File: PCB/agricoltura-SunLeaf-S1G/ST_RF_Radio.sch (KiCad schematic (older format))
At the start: 1 part

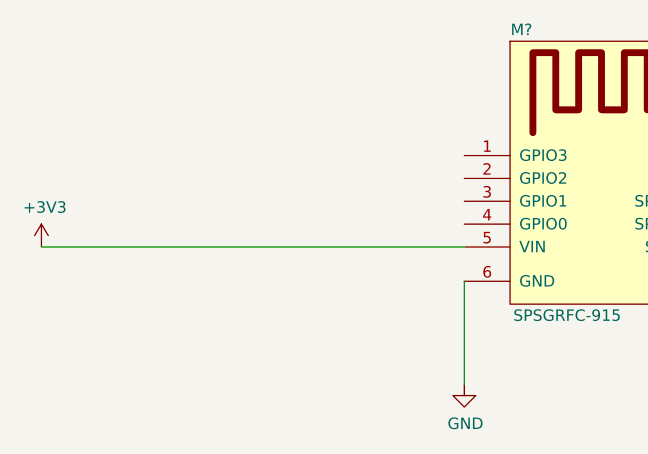
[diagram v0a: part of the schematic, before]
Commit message: Power Supply and Datasheets
Added datasheets for parts in use, designed power supply circuit
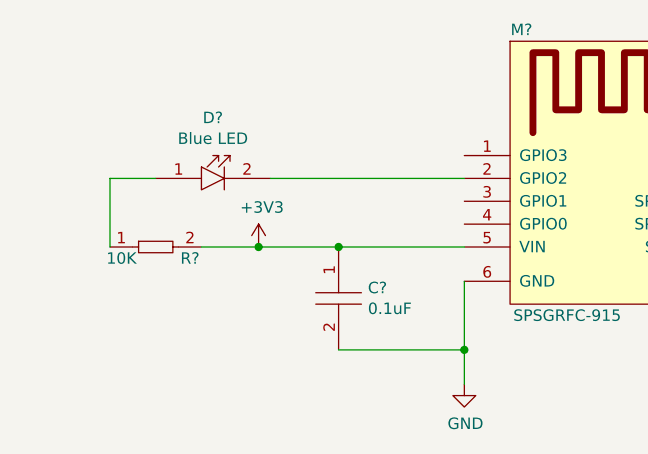
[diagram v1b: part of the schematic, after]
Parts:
- added C?: C0402C104K9PACTU, AVR-KiCAD-Lib-Resistors:R0402, symbol AVR-KiCAD-Lib-Capacitors:C0402C104K9PACTU
- added D?: LTST-C194TBKT, AVR-KiCAD-Lib-Diodes:LED0603, symbol AVR-KiCAD-Lib-Diodes:LTST-C194TBKT
- added R?: RC0402FR-0710KL, AVR-KiCAD-Lib-Resistors:R0402, symbol AVR-KiCAD-Lib-Resistors:RC0402FR-0710KL
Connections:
- net +3V3: now also C?.1, R?.2
- net GND: now also C?.2
- net at M?.2 (GPIO2): now also D?.2
- new net: D?.1, R?.1
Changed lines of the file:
@@
 	6650 3500 10350 3500
 Wire Wire Line
-	5350 3500 3500 3500
+	5350 3500 4800 3500
 $Comp
 L power:+3V3 #PWR?
 U 1 1 5F0903F3
-P 3500 3500
-F 0 "#PWR?" H 3500 3350 50  0001 C CNN
-F 1 "+3V3" H 3515 3673 50  0000 C CNN
-F 2 "" H 3500 3500 50  0001 C CNN
-F 3 "" H 3500 3500 50  0001 C CNN
-	1    3500 3500
+P 4450 3500
+F 0 "#PWR?" H 4450 3350 50  0001 C CNN
+F 1 "+3V3" H 4465 3673 50  0000 C CNN
+F 2 "" H 4450 3500 50  0001 C CNN
+F 3 "" H 4450 3500 50  0001 C CNN
+	1    4450 3500
 	1    0    0    -1
 $EndComp
@@
 $EndComp
 Wire Wire Line
-	5350 3650 5350 4100
+	5350 3650 5350 3950
+$Comp
+L AVR-KiCAD-Lib-Diodes:LTST-C194TBKT D?
+U 1 1 5F146E50
+P 4250 3200
+F 0 "D?" H 4250 3465 50  0000 C CNN
+F 1 "LTST-C194TBKT" H 4300 3400 50  0001 C CNN
+F 2 "AVR-KiCAD-Lib-Diodes:LED0603" H 4200 3050 50  0001 C CNN
+F 3 "http://optoelectronics.liteon.com/upload/download/DS22-2010-0025/LTST-C194TBKT.PDF" H 4150 3300 50  0001 C CNN
+F 4 "0.42000" H 4350 3450 50  0001 C CNN "Cost QTY: 1"
+F 5 "0.07797" H 4450 3550 50  0001 C CNN "Cost QTY: 1000"
+F 6 "*" H 4550 3650 50  0001 C CNN "Cost QTY: 2500"
+F 7 "0.06102" H 4650 3750 50  0001 C CNN "Cost QTY: 5000"
+F 8 "0.05424" H 4750 3850 50  0001 C CNN "Cost QTY: 10000"
+F 9 "Lite-On Inc." H 4850 3950 50  0001 C CNN "MFR"
+F 10 "LTST-C194TBKT" H 4950 4050 50  0001 C CNN "MFR#"
+F 11 "Digikey" H 5050 4150 50  0001 C CNN "Vendor"
+F 12 "160-1837-2-ND" H 5150 4250 50  0001 C CNN "Vendor #"
+F 13 "AVR" H 5250 4350 50  0001 C CNN "Designer"
+F 14 "0.45mm" H 5350 4450 50  0001 C CNN "Height"
+F 15 "3/1/2020" H 6450 5550 50  0001 C CNN "Date Created"
+F 16 "3/1/2020" H 5450 4550 50  0001 C CNN "Date Modified"
+F 17 "Yes" H 5550 4650 50  0001 C CNN "Lead-Free ?"
+F 18 "1" H 5650 4750 50  0001 C CNN "RoHS Levels"
+F 19 "SMT" H 5750 4850 50  0001 C CNN "Mounting"
+F 20 "2" H 5850 4950 50  0001 C CNN "Pin Count #"
+F 21 "Active" H 5950 5050 50  0001 C CNN "Status"
+F 22 "*" H 6050 5150 50  0001 C CNN "Tolerance"
+F 23 "Blue LED Colorless" H 6150 5250 50  0001 C CNN "Type"
+F 24 "3.3V" H 6250 5350 50  0001 C CNN "Voltage"
+F 25 "0603" H 6350 5500 50  0001 C CNN "Package"
+F 26 "Blue 468nm LED Indication - Discrete 3.3V 0603 (1608 Metric)" H 6650 5800 50  0001 C CNN "Description"
+F 27 "Blue LED" H 4250 3374 50  0000 C CNN "_Value_"
+F 28 "*" H 6650 5800 50  0001 C CNN "Management_ID"
+	1    4250 3200
+	1    0    0    -1
+$EndComp
+$Comp
+L AVR-KiCAD-Lib-Resistors:RC0402FR-0710KL R?
+U 1 1 5F14CD98
+P 4000 3500
+F 0 "R?" H 4150 3450 50  0000 C CNN
+F 1 "RC0402FR-0710KL" H 4000 3725 50  0001 C CNN
+F 2 "AVR-KiCAD-Lib-Resistors:R0402" H 4000 3500 50  0001 C CNN
+F 3 "https://www.yageo.com/upload/media/product/productsearch/datasheet/rchip/PYu-RC_Group_51_RoHS_L_10.pdf" H 4000 3500 50  0001 C CNN
+F 4 "0.10000" H 4100 3750 50  0001 C CNN "Cost QTY: 1"
+F 5 "0.00289" H 4200 3850 50  0001 C CNN "Cost QTY: 1000"
+F 6 "0.00251" H 4300 3950 50  0001 C CNN "Cost QTY: 2500"
+F 7 "0.00207" H 4400 4050 50  0001 C CNN "Cost QTY: 5000"
+F 8 "*" H 4500 4150 50  0001 C CNN "Cost QTY: 10000"
+F 9 "Yageo" H 4600 4250 50  0001 C CNN "MFR"
+F 10 "RC0402FR-0710KL" H 4700 4350 50  0001 C CNN "MFR#"
+F 11 "Digikey" H 4800 4450 50  0001 C CNN "Vendor"
+F 12 "311-10.0KLRCT-ND" H 4900 4550 50  0001 C CNN "Vendor #"
+F 13 "AVR" H 5000 4650 50  0001 C CNN "Designer"
+F 14 "0.4mm" H 5100 4750 50  0001 C CNN "Height"
+F 15 "12/11/2019" H 6200 5850 50  0001 C CNN "Date Created"
+F 16 "12/11/2019" H 5200 4850 50  0001 C CNN "Date Modified"
+F 17 "Yes" H 5300 4950 50  0001 C CNN "Lead-Free ?"
+F 18 "1" H 5400 5050 50  0001 C CNN "RoHS Levels"
+F 19 "SMT" H 5500 5150 50  0001 C CNN "Mounting"
+F 20 "2" H 5600 5250 50  0001 C CNN "Pin Count #"
+F 21 "Active" H 5700 5350 50  0001 C CNN "Status"
+F 22 "1%" H 5800 5450 50  0001 C CNN "Tolerance"
+F 23 "Thick FIlm Resistor" H 5900 5550 50  0001 C CNN "Type"
+F 24 "*" H 6000 5650 50  0001 C CNN "Voltage"
+F 25 "0402" H 6100 5800 50  0001 C CNN "Package"
+F 26 "10K" H 3850 3450 50  0000 C CNN "_Value_"
+F 27 "*" H 6400 6100 50  0001 C CNN "Management_ID"
+F 28 "10 kOhms ±1% 0.063W, 1/16W Chip Resistor 0402 (1005 Metric) Moisture Resistant Thick Film" H 6400 6100 50  0001 C CNN "Description"
+	1    4000 3500
+	1    0    0    -1
+$EndComp
+Wire Wire Line
+	4200 3500 4450 3500
+Connection ~ 4450 3500
+Wire Wire Line
+	3800 3500 3800 3200
+Wire Wire Line
+	3800 3200 4000 3200
+Wire Wire Line
+	4500 3200 5350 3200
+$Comp
+L AVR-KiCAD-Lib-Capacitors:C0402C104K9PACTU C?
+U 1 1 5F154BB5
+P 4800 3700
+F 0 "C?" V 4779 3828 50  0000 L CNN
+F 1 "C0402C104K9PACTU" H 4850 3900 50  0001 C CNN
+F 2 "AVR-KiCAD-Lib-Resistors:R0402" H 4600 3700 50  0001 C CNN
+F 3 "https://content.kemet.com/datasheets/KEM_C1006_X5R_SMD.pdf" H 4700 3800 50  0001 C CNN
+F 4 "0.10000" H 4900 3950 50  0001 C CNN "Cost QTY: 1"
+F 5 "0.01139" H 5000 4050 50  0001 C CNN "Cost QTY: 1000"
+F 6 "0.01035" H 5100 4150 50  0001 C CNN "Cost QTY: 2500"
+F 7 "0.00952" H 5200 4250 50  0001 C CNN "Cost QTY: 5000"
+F 8 "0.00756" H 5300 4350 50  0001 C CNN "Cost QTY: 10000"
+F 9 "KEMET" H 5400 4450 50  0001 C CNN "MFR"
+F 10 "C0402C104K9PACTU" H 5500 4550 50  0001 C CNN "MFR#"
+F 11 "Digikey" H 5600 4650 50  0001 C CNN "Vendor"
+F 12 "399-3026-6-ND" H 5700 4750 50  0001 C CNN "Vendor #"
+F 13 "AVR" H 5800 4850 50  0001 C CNN "Designer"
+F 14 "0.55mm" H 5900 4950 50  0001 C CNN "Height"
+F 15 "12/7/2019" H 7000 6050 50  0001 C CNN "Date Created"
+F 16 "12/7/2019" H 6000 5050 50  0001 C CNN "Date Modified"
+F 17 "Yes" H 6100 5150 50  0001 C CNN "Lead-Free ?"
+F 18 "1" H 6200 5250 50  0001 C CNN "RoHS Levels"
+F 19 "SMT" H 6300 5350 50  0001 C CNN "Mounting"
+F 20 "2" H 6400 5450 50  0001 C CNN "Pin Count #"
+F 21 "Active" H 6500 5550 50  0001 C CNN "Status"
+F 22 "10%" H 6600 5650 50  0001 C CNN "Tolerance"
+F 23 "Ceramic Cap" H 6700 5750 50  0001 C CNN "Type"
+F 24 "6.3V" H 6800 5850 50  0001 C CNN "Voltage"
+F 25 "0402" H 6900 6000 50  0001 C CNN "Package"
+F 26 "0.1µF ±10% 6.3V Ceramic Capacitor X5R 0402 (1005 Metric)" H 7300 6400 50  0001 C CNN "Description"
+F 27 "0.1uF" V 4870 3828 50  0000 L CNN "_Value_"
+F 28 "*" H 7200 6300 50  0001 C CNN "Management_ID"
+	1    4800 3700
+	0    1    1    0
+$EndComp
+Connection ~ 4800 3500
+Wire Wire Line
+	4800 3500 4450 3500
+Wire Wire Line
+	4800 3950 5350 3950
+Connection ~ 5350 3950
+Wire Wire Line
+	5350 3950 5350 4100
 $EndSCHEMATC

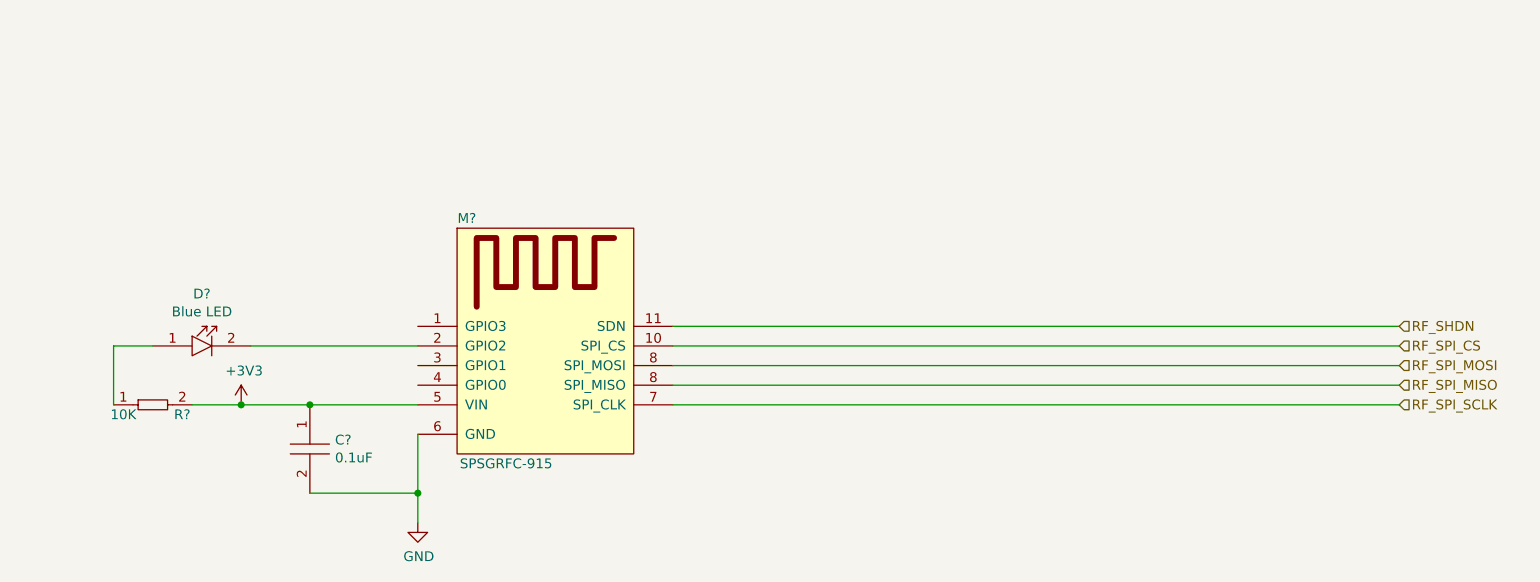
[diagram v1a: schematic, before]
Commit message: Schematic Complete
Schematic completed and PCB started
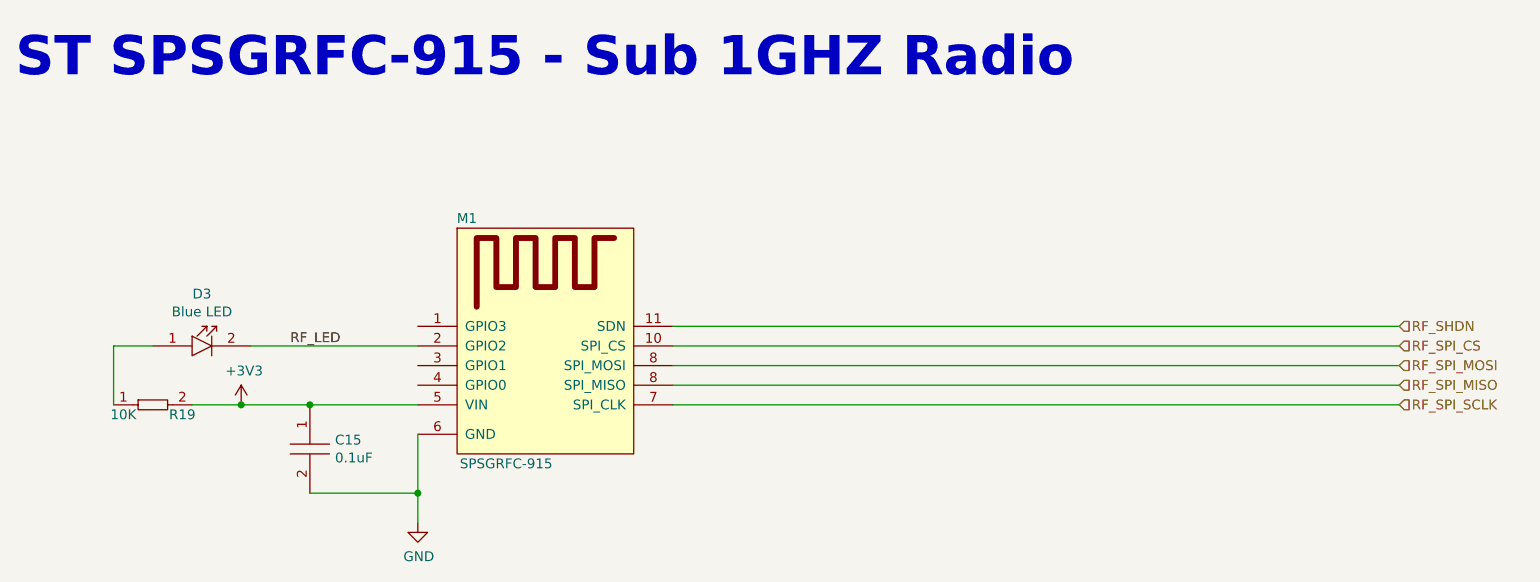
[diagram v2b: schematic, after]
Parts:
- gave numbers to parts that had none: 4
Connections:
- net RF_LED: now reaches D3.2, M1.2 (GPIO2)
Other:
- note added: "ST SPSGRFC-915 - Sub 1GHZ Radio"
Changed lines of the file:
@@
 $EndDescr
 $Comp
-L AVR-KiCAD-Lib-Modules:SPSGRFC-915 M?
+L AVR-KiCAD-Lib-Modules:SPSGRFC-915 M1
 U 1 1 5F088F18
 P 5550 2600
-F 0 "M?" H 5600 2650 50  0000 C CNN
+F 0 "M1" H 5600 2650 50  0000 C CNN
 F 1 "SPSGRFC-915" H 5600 2800 50  0001 C CNN
 F 2 "AVR-KiCAD-Lib-Modules:XCVR_SPSGRF-915" H 7600 5350 50  0001 C CNN
@@
 	5350 3500 4800 3500
 $Comp
-L power:+3V3 #PWR?
+L power:+3V3 #PWR020
 U 1 1 5F0903F3
 P 4450 3500
-F 0 "#PWR?" H 4450 3350 50  0001 C CNN
+F 0 "#PWR020" H 4450 3350 50  0001 C CNN
 F 1 "+3V3" H 4465 3673 50  0000 C CNN
 F 2 "" H 4450 3500 50  0001 C CNN
@@
 $EndComp
 $Comp
-L power:GND #PWR?
+L power:GND #PWR021
 U 1 1 5F090A88
 P 5350 4100
-F 0 "#PWR?" H 5350 3850 50  0001 C CNN
+F 0 "#PWR021" H 5350 3850 50  0001 C CNN
 F 1 "GND" H 5355 3927 50  0000 C CNN
 F 2 "" H 5350 4100 50  0001 C CNN
@@
 	5350 3650 5350 3950
 $Comp
-L AVR-KiCAD-Lib-Diodes:LTST-C194TBKT D?
+L AVR-KiCAD-Lib-Diodes:LTST-C194TBKT D3
 U 1 1 5F146E50
 P 4250 3200
-F 0 "D?" H 4250 3465 50  0000 C CNN
+F 0 "D3" H 4250 3465 50  0000 C CNN
 F 1 "LTST-C194TBKT" H 4300 3400 50  0001 C CNN
 F 2 "AVR-KiCAD-Lib-Diodes:LED0603" H 4200 3050 50  0001 C CNN
@@
 $EndComp
 $Comp
-L AVR-KiCAD-Lib-Resistors:RC0402FR-0710KL R?
+L AVR-KiCAD-Lib-Resistors:RC0402FR-0710KL R19
 U 1 1 5F14CD98
 P 4000 3500
-F 0 "R?" H 4150 3450 50  0000 C CNN
+F 0 "R19" H 4150 3450 50  0000 C CNN
 F 1 "RC0402FR-0710KL" H 4000 3725 50  0001 C CNN
 F 2 "AVR-KiCAD-Lib-Resistors:R0402" H 4000 3500 50  0001 C CNN
@@
 	4500 3200 5350 3200
 $Comp
-L AVR-KiCAD-Lib-Capacitors:C0402C104K9PACTU C?
+L AVR-KiCAD-Lib-Capacitors:C0402C104K9PACTU C15
 U 1 1 5F154BB5
 P 4800 3700
-F 0 "C?" V 4779 3828 50  0000 L CNN
+F 0 "C15" V 4779 3828 50  0000 L CNN
 F 1 "C0402C104K9PACTU" H 4850 3900 50  0001 C CNN
 F 2 "AVR-KiCAD-Lib-Resistors:R0402" H 4600 3700 50  0001 C CNN
@@
 Wire Wire Line
 	5350 3950 5350 4100
+Text Label 4700 3200 0    50   ~ 0
+RF_LED
+Text Notes 3300 1850 0    200  ~ 40
+ST SPSGRFC-915 - Sub 1GHZ Radio
 $EndSCHEMATC

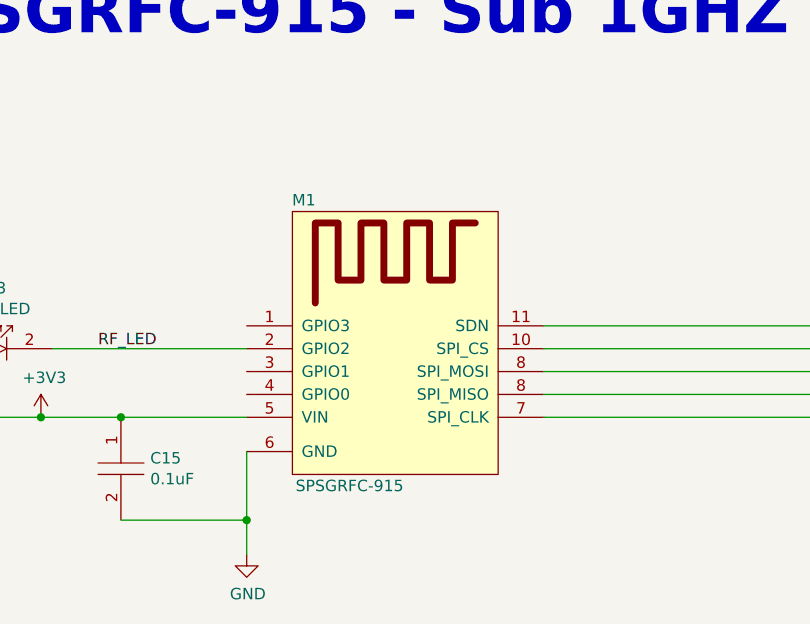
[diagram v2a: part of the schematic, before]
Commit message: PCB Progress
added TVS diodes fo QWIIC connector serial signals. Did more routing overall.
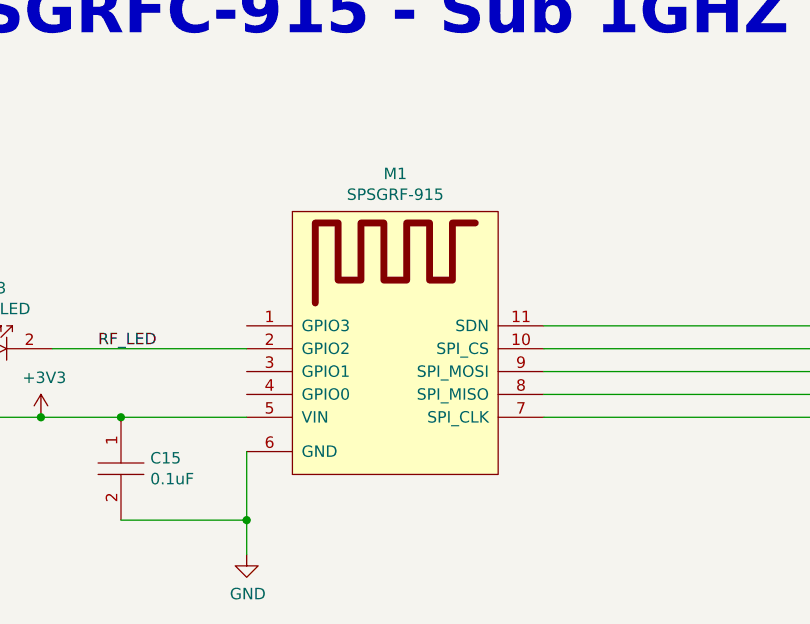
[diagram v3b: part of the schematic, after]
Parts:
- removed M1: SPSGRFC-915, AVR-KiCAD-Lib-Modules:XCVR_SPSGRF-915, symbol AVR-KiCAD-Lib-Modules:SPSGRFC-915
- added M1: SPSGRF-915, AVR-KiCAD-Lib-Modules:XCVR_SPSGRF-915, symbol AVR-KiCAD-Lib-Modules:SPSGRF-915
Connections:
- net +3V3: now also M1.5 (VIN)
- net GND: now also M1.6 (GND)
- net RF_LED: now also M1.2 (GPIO2)
- net RF_SHDN: now also M1.11 (SDN)
- net RF_SPI_CS: now also M1.10 (SPI_CS)
- net RF_SPI_MISO: now also M1.8 (SPI_MISO)
- net RF_SPI_MOSI: now also M1.9 (SPI_MOSI)
- net RF_SPI_SCLK: now also M1.7 (SPI_CLK)
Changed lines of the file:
@@
 Comment4 ""
 $EndDescr
-$Comp
-L AVR-KiCAD-Lib-Modules:SPSGRFC-915 M1
-U 1 1 5F088F18
-P 5550 2600
-F 0 "M1" H 5600 2650 50  0000 C CNN
-F 1 "SPSGRFC-915" H 5600 2800 50  0001 C CNN
-F 2 "AVR-KiCAD-Lib-Modules:XCVR_SPSGRF-915" H 7600 5350 50  0001 C CNN
-F 3 "https://www.st.com/content/ccc/resource/technical/document/datasheet/group3/21/ae/a6/78/64/3b/46/5d/DM00347814/files/DM00347814.pdf/jcr:content/translations/en.DM00347814.pdf" H 5450 2700 50  0001 C CNN
-F 4 "12.35000" H 5650 2850 50  0001 C CNN "Cost QTY: 1"
-F 5 "7.82040" H 5750 2950 50  0001 C CNN "Cost QTY: 1000"
-F 6 "*" H 5850 3050 50  0001 C CNN "Cost QTY: 2500"
-F 7 "7.29120" H 5950 3150 50  0001 C CNN "Cost QTY: 5000"
-F 8 "7.05600" H 6050 3250 50  0001 C CNN "Cost QTY: 10000"
-F 9 "STMicroelectronics" H 6150 3350 50  0001 C CNN "MFR"
-F 10 "SPSGRFC-915" H 6250 3450 50  0001 C CNN "MFR#"
-F 11 "Digikey" H 6350 3550 50  0001 C CNN "Vendor"
-F 12 "497-17226-ND" H 6450 3650 50  0001 C CNN "Vendor #"
-F 13 "AVR" H 6550 3750 50  0001 C CNN "Designer"
-F 14 "2mm" H 6650 3850 50  0001 C CNN "Height"
-F 15 "6/4/2020" H 7750 4950 50  0001 C CNN "Date Created"
-F 16 "6/4/2020" H 6750 3950 50  0001 C CNN "Date Modified"
-F 17 "Yes" H 6850 4050 50  0001 C CNN "Lead-Free ?"
-F 18 "1" H 6950 4150 50  0001 C CNN "RoHS Levels"
-F 19 "SMT" H 7050 4250 50  0001 C CNN "Mounting"
-F 20 "11" H 7150 4350 50  0001 C CNN "Pin Count #"
-F 21 "Active" H 7250 4450 50  0001 C CNN "Status"
-F 22 "*" H 7350 4550 50  0001 C CNN "Tolerance"
-F 23 "SoM" H 7450 4650 50  0001 C CNN "Type"
-F 24 "1.8V ~ 3.6V" H 7550 4750 50  0001 C CNN "Voltage"
-F 25 "Proprietary Module" H 7650 4900 50  0001 C CNN "Package"
-F 26 "General ISM < 1GHz  Transceiver Module 433MHz, 868MHz, 915MHz Antenna Not Included, U.FL Surface Mount" H 7950 5200 50  0001 C CNN "Description"
-F 27 "SPSGRFC-915" H 5800 1400 50  0000 C CNN "_Value_"
-F 28 "*" H 7950 5200 50  0001 C CNN "Management_ID"
-	1    5550 2600
-	1    0    0    -1
-$EndComp
 Text HLabel 10350 3100 2    50   Input ~ 0
 RF_SHDN
@@
 Text Notes 3300 1850 0    200  ~ 40
 ST SPSGRFC-915 - Sub 1GHZ Radio
+$Comp
+L AVR-KiCAD-Lib-Modules:SPSGRF-915 M1
+U 1 1 5F42ADCA
+P 5550 2600
+F 0 "M1" H 6000 2765 50  0000 C CNN
+F 1 "SPSGRF-915" H 5600 2800 50  0001 C CNN
+F 2 "AVR-KiCAD-Lib-Modules:XCVR_SPSGRF-915" H 7600 5350 50  0001 C CNN
+F 3 "https://www.st.com/content/ccc/resource/technical/document/datasheet/f9/a3/aa/67/de/86/4b/62/DM00171035.pdf/files/DM00171035.pdf/jcr:content/translations/en.DM00171035.pdf" H 5450 2700 50  0001 C CNN
+F 4 "15.79000" H 5650 2850 50  0001 C CNN "Cost QTY: 1"
+F 5 "10.00160" H 5750 2950 50  0001 C CNN "Cost QTY: 1000"
+F 6 "*" H 5850 3050 50  0001 C CNN "Cost QTY: 2500"
+F 7 "9.32480" H 5950 3150 50  0001 C CNN "Cost QTY: 5000"
+F 8 "9.02400" H 6050 3250 50  0001 C CNN "Cost QTY: 10000"
+F 9 "STMicroelectronics" H 6150 3350 50  0001 C CNN "MFR"
+F 10 "SPSGRF-915" H 6250 3450 50  0001 C CNN "MFR#"
+F 11 "Digikey" H 6350 3550 50  0001 C CNN "Vendor"
+F 12 "497-15956-ND" H 6450 3650 50  0001 C CNN "Vendor #"
+F 13 "AVR" H 6550 3750 50  0001 C CNN "Designer"
+F 14 "2mm" H 6650 3850 50  0001 C CNN "Height"
+F 15 "6/4/2020" H 7750 4950 50  0001 C CNN "Date Created"
+F 16 "6/4/2020" H 6750 3950 50  0001 C CNN "Date Modified"
+F 17 "Yes" H 6850 4050 50  0001 C CNN "Lead-Free ?"
+F 18 "1" H 6950 4150 50  0001 C CNN "RoHS Levels"
+F 19 "SMT" H 7050 4250 50  0001 C CNN "Mounting"
+F 20 "11" H 7150 4350 50  0001 C CNN "Pin Count #"
+F 21 "Active" H 7250 4450 50  0001 C CNN "Status"
+F 22 "*" H 7350 4550 50  0001 C CNN "Tolerance"
+F 23 "SoM" H 7450 4650 50  0001 C CNN "Type"
+F 24 "1.8V ~ 3.6V" H 7550 4750 50  0001 C CNN "Voltage"
+F 25 "Proprietary Module" H 7650 4900 50  0001 C CNN "Package"
+F 26 "General ISM < 1GHz  Transceiver Module 915MHz Integrated, Chip Surface Mount" H 7950 5200 50  0001 C CNN "Description"
+F 27 "SPSGRF-915" H 6000 2674 50  0000 C CNN "_Value_"
+F 28 "*" H 7950 5200 50  0001 C CNN "Management_ID"
+	1    5550 2600
+	1    0    0    -1
+$EndComp
 $EndSCHEMATC
